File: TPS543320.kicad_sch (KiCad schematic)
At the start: 19 parts, among them U11 TPS543320RPYR

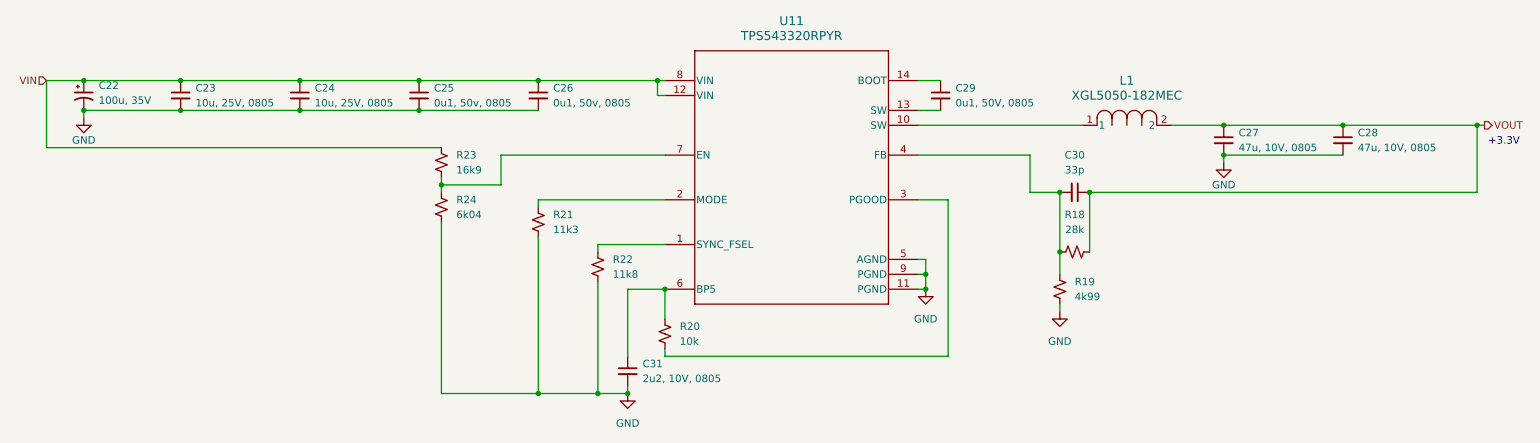
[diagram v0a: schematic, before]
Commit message: OBC: initial schematic entry complete
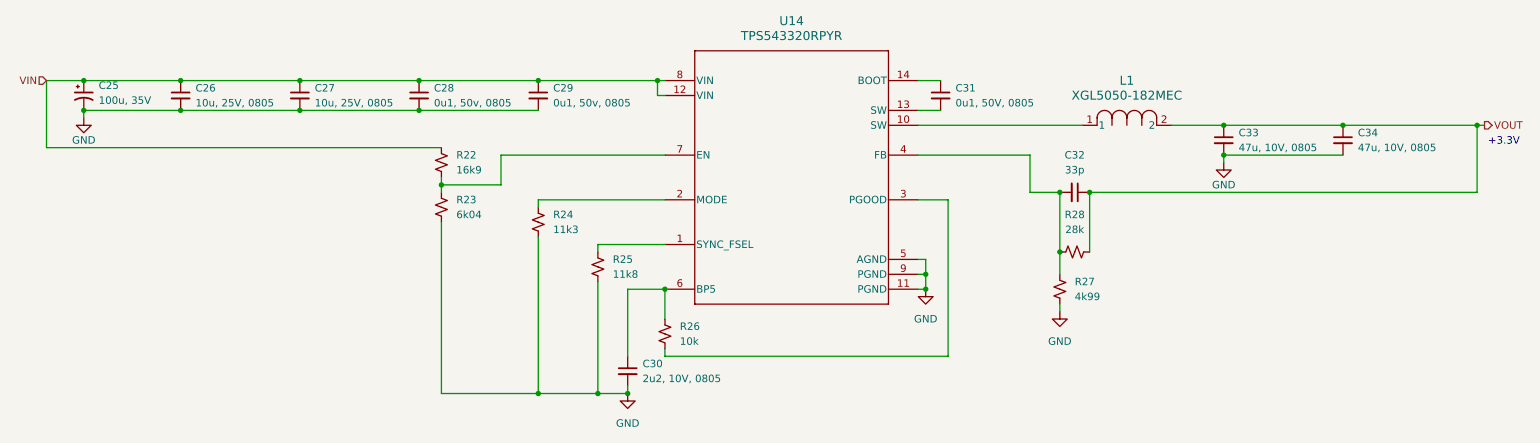
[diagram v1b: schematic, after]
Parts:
- C26: renamed from C23; footprint (none) -> Capacitor_SMD:C_0805_2012Metric
- C27: renamed from C24; footprint (none) -> Capacitor_SMD:C_0805_2012Metric
- C28: renamed from C25; footprint (none) -> Capacitor_SMD:C_0805_2012Metric
- C29: renamed from C26; footprint (none) -> Capacitor_SMD:C_0805_2012Metric
- C30: renamed from C31; footprint (none) -> Capacitor_SMD:C_0805_2012Metric
- C31: renamed from C29; footprint (none) -> Capacitor_SMD:C_0805_2012Metric
- C32: renamed from C30; footprint (none) -> Capacitor_SMD:C_0805_2012Metric
- C33: renamed from C27; footprint (none) -> Capacitor_SMD:C_0805_2012Metric
- C34: renamed from C28; footprint (none) -> Capacitor_SMD:C_0805_2012Metric
- R22: renamed from R23; footprint (none) -> Resistor_SMD:R_0805_2012Metric
- R23: renamed from R24; footprint (none) -> Resistor_SMD:R_0805_2012Metric
- R24: renamed from R21; footprint (none) -> Resistor_SMD:R_0805_2012Metric
- R25: renamed from R22; footprint (none) -> Resistor_SMD:R_0805_2012Metric
- R26: renamed from R20; footprint (none) -> Resistor_SMD:R_0805_2012Metric
- R27: renamed from R19; footprint (none) -> Resistor_SMD:R_0805_2012Metric
- R28: renamed from R18; footprint (none) -> Resistor_SMD:R_0805_2012Metric
- renumbered C22 to C25, U11 to U14

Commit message: OBC: preliminary layout
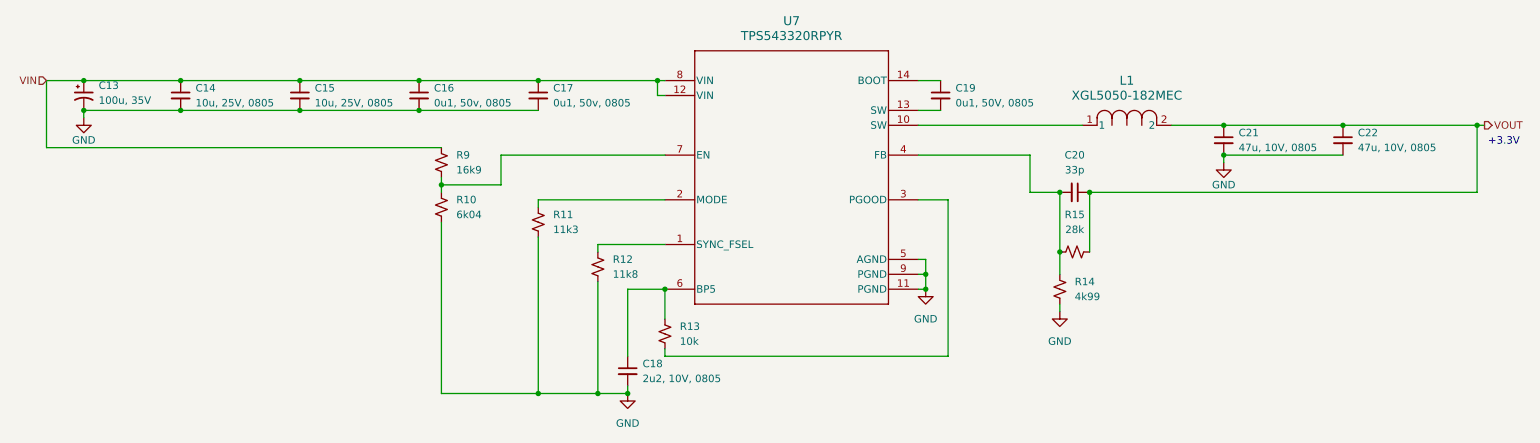
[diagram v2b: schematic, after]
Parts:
- C13: renamed from C25; footprint (none) -> Capacitor_SMD:C_0805_2012Metric
- L1: footprint IND_XGL5050_COC -> XGL5050-182MEC:IND_XGL5050_COC
- U7: renamed from U14; footprint RPY0014A-MFG -> TPS543320RPYR:RPY0014A-MFG
- renumbered C26 to C14, C27 to C15, C28 to C16, C29 to C17, C30 to C18, C31 to C19, C32 to C20, C33 to C21, C34 to C22, R23 to R10, R24 to R11, R25 to R12, R26 to R13, R27 to R14, R28 to R15, R22 to R9
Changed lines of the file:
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@@
 		(dnp no)
 		(fields_autoplaced yes)
-		(property "Reference" "C25"
+		(property "Reference" "C13"
 			(at 99.06 117.6781 0)
 			(effects
@@
 			)
 		)
-		(property "Footprint" ""
+		(property "Footprint" "Capacitor_SMD:C_0805_2012Metric"
 			(at 96.52 119.38 0)
 			(effects
@@
 			(project ""
 				(path "/ace5002f-3cbc-4a0a-869b-0e31ebd905b7/893aef5a-59ff-410b-9a71-9930aaf04e9f/e2cad078-3ca5-46c7-a65f-c1e6fb9d60cb"
-					(reference "C25")
+					(reference "C13")
 					(unit 1)
 				)
@@
 		(dnp no)
 		(fields_autoplaced yes)
-		(property "Reference" "R25"
+		(property "Reference" "R12"
 			(at 186.69 147.3199 0)
 			(effects
@@
 			(project ""
 				(path "/ace5002f-3cbc-4a0a-869b-0e31ebd905b7/893aef5a-59ff-410b-9a71-9930aaf04e9f/e2cad078-3ca5-46c7-a65f-c1e6fb9d60cb"
-					(reference "R25")
+					(reference "R12")
 					(unit 1)
 				)
@@
 		(dnp no)
 		(fields_autoplaced yes)
-		(property "Reference" "#PWR0102"
+		(property "Reference" "#PWR054"
 			(at 189.23 176.53 0)
 			(effects
@@
 			(project "Avionics"
 				(path "/ace5002f-3cbc-4a0a-869b-0e31ebd905b7/893aef5a-59ff-410b-9a71-9930aaf04e9f/e2cad078-3ca5-46c7-a65f-c1e6fb9d60cb"
-					(reference "#PWR0102")
+					(reference "#PWR054")
 					(unit 1)
 				)
@@
 		(dnp no)
 		(fields_autoplaced yes)
-		(property "Reference" "#PWR0104"
+		(property "Reference" "#PWR056"
 			(at 262.89 162.56 0)
 			(effects
@@
 			(project "Avionics"
 				(path "/ace5002f-3cbc-4a0a-869b-0e31ebd905b7/893aef5a-59ff-410b-9a71-9930aaf04e9f/e2cad078-3ca5-46c7-a65f-c1e6fb9d60cb"
-					(reference "#PWR0104")
+					(reference "#PWR056")
 					(unit 1)
 				)
@@
 		(dnp no)
 		(fields_autoplaced yes)
-		(property "Reference" "R23"
+		(property "Reference" "R10"
 			(at 160.02 137.1599 0)
 			(effects
@@
 			(project ""
 				(path "/ace5002f-3cbc-4a0a-869b-0e31ebd905b7/893aef5a-59ff-410b-9a71-9930aaf04e9f/e2cad078-3ca5-46c7-a65f-c1e6fb9d60cb"
-					(reference "R23")
+					(reference "R10")
 					(unit 1)
 				)
@@
 		(on_board yes)
 		(dnp no)
-		(property "Reference" "#PWR0101"
+		(property "Reference" "#PWR053"
 			(at 96.52 129.54 0)
 			(effects
@@
 			(project ""
 				(path "/ace5002f-3cbc-4a0a-869b-0e31ebd905b7/893aef5a-59ff-410b-9a71-9930aaf04e9f/e2cad078-3ca5-46c7-a65f-c1e6fb9d60cb"
-					(reference "#PWR0101")
+					(reference "#PWR053")
 					(unit 1)
 				)
@@
 		(dnp no)
 		(fields_autoplaced yes)
-		(property "Reference" "R24"
+		(property "Reference" "R11"
 			(at 176.53 139.6999 0)
 			(effects
@@
 			(project ""
 				(path "/ace5002f-3cbc-4a0a-869b-0e31ebd905b7/893aef5a-59ff-410b-9a71-9930aaf04e9f/e2cad078-3ca5-46c7-a65f-c1e6fb9d60cb"
-					(reference "R24")
+					(reference "R11")
 					(unit 1)
 				)
@@
 		(dnp no)
 		(fields_autoplaced yes)
-		(property "Reference" "C33"
+		(property "Reference" "C21"
 			(at 293.37 125.7362 0)
 			(effects
@@
 			(project ""
 				(path "/ace5002f-3cbc-4a0a-869b-0e31ebd905b7/893aef5a-59ff-410b-9a71-9930aaf04e9f/e2cad078-3ca5-46c7-a65f-c1e6fb9d60cb"
-					(reference "C33")
+					(reference "C21")
 					(unit 1)
 				)
@@
 		(dnp no)
 		(fields_autoplaced yes)
-		(property "Reference" "C31"
+		(property "Reference" "C19"
 			(at 245.11 118.1162 0)
 			(effects
@@
 			(project ""
 				(path "/ace5002f-3cbc-4a0a-869b-0e31ebd905b7/893aef5a-59ff-410b-9a71-9930aaf04e9f/e2cad078-3ca5-46c7-a65f-c1e6fb9d60cb"
-					(reference "C31")
+					(reference "C19")
 					(unit 1)
 				)
@@
 		(dnp no)
 		(fields_autoplaced yes)
-		(property "Reference" "R22"
+		(property "Reference" "R9"
 			(at 160.02 129.5399 0)
 			(effects
@@
 			(project ""
 				(path "/ace5002f-3cbc-4a0a-869b-0e31ebd905b7/893aef5a-59ff-410b-9a71-9930aaf04e9f/e2cad078-3ca5-46c7-a65f-c1e6fb9d60cb"
-					(reference "R22")
+					(reference "R9")
 					(unit 1)
 				)
@@
 		(dnp no)
 		(fields_autoplaced yes)
-		(property "Reference" "C30"
+		(property "Reference" "C18"
 			(at 191.77 165.1062 0)
 			(effects
@@
 			(project ""
 				(path "/ace5002f-3cbc-4a0a-869b-0e31ebd905b7/893aef5a-59ff-410b-9a71-9930aaf04e9f/e2cad078-3ca5-46c7-a65f-c1e6fb9d60cb"
-					(reference "C30")
+					(reference "C18")
 					(unit 1)
 				)
@@
 		(dnp no)
 		(fields_autoplaced yes)
-		(property "Reference" "C29"
+		(property "Reference" "C17"
 			(at 176.53 118.1162 0)
 			(effects
@@
 			(project ""
 				(path "/ace5002f-3cbc-4a0a-869b-0e31ebd905b7/893aef5a-59ff-410b-9a71-9930aaf04e9f/e2cad078-3ca5-46c7-a65f-c1e6fb9d60cb"
-					(reference "C29")
+					(reference "C17")
 					(unit 1)
 				)
@@
 		(dnp no)
 		(fields_autoplaced yes)
-		(property "Reference" "R28"
+		(property "Reference" "R15"
 			(at 265.43 139.7 90)
 			(effects
@@
 			(project ""
 				(path "/ace5002f-3cbc-4a0a-869b-0e31ebd905b7/893aef5a-59ff-410b-9a71-9930aaf04e9f/e2cad078-3ca5-46c7-a65f-c1e6fb9d60cb"
-					(reference "R28")
+					(reference "R15")
 					(unit 1)
 				)
@@
 		(dnp no)
 		(fields_autoplaced yes)
-		(property "Reference" "R27"
+		(property "Reference" "R14"
 			(at 265.43 151.1299 0)
 			(effects
@@
 			(project ""
 				(path "/ace5002f-3cbc-4a0a-869b-0e31ebd905b7/893aef5a-59ff-410b-9a71-9930aaf04e9f/e2cad078-3ca5-46c7-a65f-c1e6fb9d60cb"
-					(reference "R27")
+					(reference "R14")
 					(unit 1)
 				)
@@
 		(dnp no)
 		(fields_autoplaced yes)
-		(property "Reference" "U14"
+		(property "Reference" "U7"
 			(at 217.17 106.68 0)
 			(effects
@@
 			)
 		)
-		(property "Footprint" "RPY0014A-MFG"
+		(property "Footprint" "TPS543320RPYR:RPY0014A-MFG"
 			(at 195.58 116.84 0)
 			(effects
@@
 			(project "Avionics"
 				(path "/ace5002f-3cbc-4a0a-869b-0e31ebd905b7/893aef5a-59ff-410b-9a71-9930aaf04e9f/e2cad078-3ca5-46c7-a65f-c1e6fb9d60cb"
-					(reference "U14")
+					(reference "U7")
 					(unit 1)
 				)
@@
 		(on_board yes)
 		(dnp no)
-		(property "Reference" "#PWR0105"
+		(property "Reference" "#PWR057"
 			(at 290.83 137.16 0)
 			(effects
@@
 			(project ""
 				(path "/ace5002f-3cbc-4a0a-869b-0e31ebd905b7/893aef5a-59ff-410b-9a71-9930aaf04e9f/e2cad078-3ca5-46c7-a65f-c1e6fb9d60cb"
-					(reference "#PWR0105")
+					(reference "#PWR057")
 					(unit 1)
 				)
@@
 		(dnp no)
 		(fields_autoplaced yes)
-		(property "Reference" "C26"
+		(property "Reference" "C14"
 			(at 115.57 118.1162 0)
 			(effects
@@
 			(project ""
 				(path "/ace5002f-3cbc-4a0a-869b-0e31ebd905b7/893aef5a-59ff-410b-9a71-9930aaf04e9f/e2cad078-3ca5-46c7-a65f-c1e6fb9d60cb"
-					(reference "C26")
+					(reference "C14")
 					(unit 1)
 				)
@@
 		(dnp no)
 		(fields_autoplaced yes)
-		(property "Reference" "C32"
+		(property "Reference" "C20"
 			(at 265.4236 129.54 90)
 			(effects
@@
 			(project "Avionics"
 				(path "/ace5002f-3cbc-4a0a-869b-0e31ebd905b7/893aef5a-59ff-410b-9a71-9930aaf04e9f/e2cad078-3ca5-46c7-a65f-c1e6fb9d60cb"
-					(reference "C32")
+					(reference "C20")
 					(unit 1)
 				)
@@
 			)
 		)
-		(property "Footprint" "IND_XGL5050_COC"
+		(property "Footprint" "XGL5050-182MEC:IND_XGL5050_COC"
 			(at 281.94 124.46 0)
 			(effects
@@
 		(on_board yes)
 		(dnp no)
-		(property "Reference" "C28"
+		(property "Reference" "C16"
 			(at 156.21 118.1162 0)
 			(effects
@@
 			(project ""
 				(path "/ace5002f-3cbc-4a0a-869b-0e31ebd905b7/893aef5a-59ff-410b-9a71-9930aaf04e9f/e2cad078-3ca5-46c7-a65f-c1e6fb9d60cb"
-					(reference "C28")
+					(reference "C16")
 					(unit 1)
 				)
@@
 		(dnp no)
 		(fields_autoplaced yes)
-		(property "Reference" "C27"
+		(property "Reference" "C15"
 			(at 135.89 118.1162 0)
 			(effects
@@
 			(project ""
 				(path "/ace5002f-3cbc-4a0a-869b-0e31ebd905b7/893aef5a-59ff-410b-9a71-9930aaf04e9f/e2cad078-3ca5-46c7-a65f-c1e6fb9d60cb"
-					(reference "C27")
+					(reference "C15")
 					(unit 1)
 				)
@@
 		(dnp no)
 		(fields_autoplaced yes)
-		(property "Reference" "R26"
+		(property "Reference" "R13"
 			(at 198.12 158.7499 0)
 			(effects
@@
 			(project ""
 				(path "/ace5002f-3cbc-4a0a-869b-0e31ebd905b7/893aef5a-59ff-410b-9a71-9930aaf04e9f/e2cad078-3ca5-46c7-a65f-c1e6fb9d60cb"
-					(reference "R26")
+					(reference "R13")
 					(unit 1)
 				)
@@
 		(dnp no)
 		(fields_autoplaced yes)
-		(property "Reference" "C34"
+		(property "Reference" "C22"
 			(at 313.69 125.7362 0)
 			(effects
@@
 			(project ""
 				(path "/ace5002f-3cbc-4a0a-869b-0e31ebd905b7/893aef5a-59ff-410b-9a71-9930aaf04e9f/e2cad078-3ca5-46c7-a65f-c1e6fb9d60cb"
-					(reference "C34")
+					(reference "C22")
 					(unit 1)
 				)
@@
 		(dnp no)
 		(fields_autoplaced yes)
-		(property "Reference" "#PWR0103"
+		(property "Reference" "#PWR055"
 			(at 240.03 158.75 0)
 			(effects
@@
 			(project ""
 				(path "/ace5002f-3cbc-4a0a-869b-0e31ebd905b7/893aef5a-59ff-410b-9a71-9930aaf04e9f/e2cad078-3ca5-46c7-a65f-c1e6fb9d60cb"
-					(reference "#PWR0103")
-					(unit 1)
-				)
+					(reference "#PWR055")
+					(unit 1)
+				)

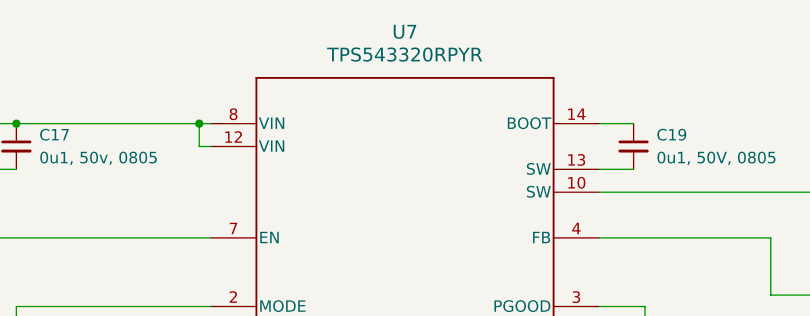
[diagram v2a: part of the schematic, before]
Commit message: OBC: start PCB layout
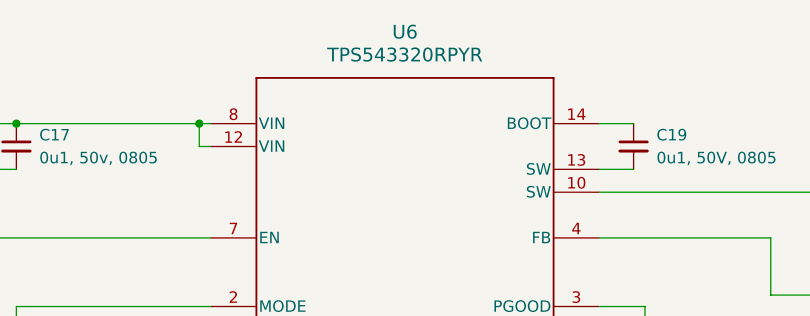
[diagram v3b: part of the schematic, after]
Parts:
- renumbered U7 to U6
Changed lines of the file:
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@@
 		(dnp no)
 		(fields_autoplaced yes)
-		(property "Reference" "#PWR054"
+		(property "Reference" "#PWR055"
 			(at 189.23 176.53 0)
 			(effects
@@
 			(project "Avionics"
 				(path "/ace5002f-3cbc-4a0a-869b-0e31ebd905b7/893aef5a-59ff-410b-9a71-9930aaf04e9f/e2cad078-3ca5-46c7-a65f-c1e6fb9d60cb"
-					(reference "#PWR054")
+					(reference "#PWR055")
 					(unit 1)
 				)
@@
 		(dnp no)
 		(fields_autoplaced yes)
-		(property "Reference" "#PWR056"
+		(property "Reference" "#PWR057"
 			(at 262.89 162.56 0)
 			(effects
@@
 			(project "Avionics"
 				(path "/ace5002f-3cbc-4a0a-869b-0e31ebd905b7/893aef5a-59ff-410b-9a71-9930aaf04e9f/e2cad078-3ca5-46c7-a65f-c1e6fb9d60cb"
-					(reference "#PWR056")
+					(reference "#PWR057")
 					(unit 1)
 				)
@@
 		(on_board yes)
 		(dnp no)
-		(property "Reference" "#PWR053"
+		(property "Reference" "#PWR054"
 			(at 96.52 129.54 0)
 			(effects
@@
 			(project ""
 				(path "/ace5002f-3cbc-4a0a-869b-0e31ebd905b7/893aef5a-59ff-410b-9a71-9930aaf04e9f/e2cad078-3ca5-46c7-a65f-c1e6fb9d60cb"
-					(reference "#PWR053")
+					(reference "#PWR054")
 					(unit 1)
 				)
@@
 		(dnp no)
 		(fields_autoplaced yes)
-		(property "Reference" "U7"
+		(property "Reference" "U6"
 			(at 217.17 106.68 0)
 			(effects
@@
 			(project "Avionics"
 				(path "/ace5002f-3cbc-4a0a-869b-0e31ebd905b7/893aef5a-59ff-410b-9a71-9930aaf04e9f/e2cad078-3ca5-46c7-a65f-c1e6fb9d60cb"
-					(reference "U7")
+					(reference "U6")
 					(unit 1)
 				)
@@
 		(on_board yes)
 		(dnp no)
-		(property "Reference" "#PWR057"
+		(property "Reference" "#PWR058"
 			(at 290.83 137.16 0)
 			(effects
@@
 			(project ""
 				(path "/ace5002f-3cbc-4a0a-869b-0e31ebd905b7/893aef5a-59ff-410b-9a71-9930aaf04e9f/e2cad078-3ca5-46c7-a65f-c1e6fb9d60cb"
-					(reference "#PWR057")
+					(reference "#PWR058")
 					(unit 1)
 				)
@@
 		(dnp no)
 		(fields_autoplaced yes)
-		(property "Reference" "#PWR055"
+		(property "Reference" "#PWR056"
 			(at 240.03 158.75 0)
 			(effects
@@
 			(project ""
 				(path "/ace5002f-3cbc-4a0a-869b-0e31ebd905b7/893aef5a-59ff-410b-9a71-9930aaf04e9f/e2cad078-3ca5-46c7-a65f-c1e6fb9d60cb"
-					(reference "#PWR055")
-					(unit 1)
-				)
+					(reference "#PWR056")
+					(unit 1)
+				)

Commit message: OBC: Continue PCB lauout
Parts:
- renumbered C14 to C10, C15 to C11, C16 to C12, C17 to C13, C18 to C14, C19 to C15, C20 to C16, C21 to C17, C22 to C18, C13 to C9, R9 to R11, R10 to R12, R11 to R13, R12 to R14, R13 to R15, R14 to R16, R15 to R17, U6 to U5

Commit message: Layout confirmed, PCBs ordered
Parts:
- C10, C11: DigiKey Part Number (none) -> 490-GRM21BZ71E106KE15KCT-ND
- C12, C13, C15: DigiKey Part Number (none) -> 399-C0805C104K5RACTUCT-ND
- C14: DigiKey Part Number (none) -> 1276-CL21B225KPFVPNECT-ND
- C16: DigiKey Part Number (none) -> 490-14776-1-ND
- C17, C18: DigiKey Part Number (none) -> 490-9961-1-ND
- C9: DigiKey Part Number (none) -> 399-C0805X104K5RAC7210CT-ND
- L1: DigiKey Part Number (none) -> 2457-XGL5050-182MEC-ND
- R11: DigiKey Part Number (none) -> 311-16.9KCRCT-ND
- R12: DigiKey Part Number (none) -> RMCF0805FT6K04CT-ND
- R13: DigiKey Part Number (none) -> 311-11.3KCRCT-ND
- R14: DigiKey Part Number (none) -> RMCF0805FT11K8CT-ND
- R15: DigiKey Part Number (none) -> 541-10.0KCCT-ND
- R16: DigiKey Part Number (none) -> TNP4.99KABCT-ND
- R17: DigiKey Part Number (none) -> 311-28.0KCRCT-ND
- U5: DigiKey Part Number (none) -> 296-TPS543320RPYRCT-ND
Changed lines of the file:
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@@
+			)
+		)
+		(property "DigiKey Part Number" "399-C0805X104K5RAC7210CT-ND"
+			(at 96.52 119.38 0)
+			(effects
+				(font
+					(size 1.27 1.27)
+				)
+				(hide yes)
 			)
 		)
@@
 			)
 		)
+		(property "DigiKey Part Number" "RMCF0805FT11K8CT-ND"
+			(at 184.15 148.59 0)
+			(effects
+				(font
+					(size 1.27 1.27)
+				)
+				(hide yes)
+			)
+		)
 		(pin "2"
 		)
@@
 			)
 		)
+		(property "DigiKey Part Number" "RMCF0805FT6K04CT-ND"
+			(at 157.48 138.43 0)
+			(effects
+				(font
+					(size 1.27 1.27)
+				)
+				(hide yes)
+			)
+		)
 		(pin "2"
 		)
@@
 			)
 		)
+		(property "DigiKey Part Number" "311-11.3KCRCT-ND"
+			(at 173.99 140.97 0)
+			(effects
+				(font
+					(size 1.27 1.27)
+				)
+				(hide yes)
+			)
+		)
 		(pin "2"
 		)
@@
 			)
 		)
+		(property "DigiKey Part Number" "490-9961-1-ND"
+			(at 290.83 127 0)
+			(effects
+				(font
+					(size 1.27 1.27)
+				)
+				(hide yes)
+			)
+		)
 		(pin "2"
 		)
@@
 			)
 		)
+		(property "DigiKey Part Number" "399-C0805C104K5RACTUCT-ND"
+			(at 242.57 119.38 0)
+			(effects
+				(font
+					(size 1.27 1.27)
+				)
+				(hide yes)
+			)
+		)
 		(pin "1"
 		)
@@
 			)
 		)
+		(property "DigiKey Part Number" "311-16.9KCRCT-ND"
+			(at 157.48 130.81 0)
+			(effects
+				(font
+					(size 1.27 1.27)
+				)
+				(hide yes)
+			)
+		)
 		(pin "2"
 		)
@@
 			)
 		)
+		(property "DigiKey Part Number" "1276-CL21B225KPFVPNECT-ND"
+			(at 189.23 166.37 0)
+			(effects
+				(font
+					(size 1.27 1.27)
+				)
+				(hide yes)
+			)
+		)
 		(pin "1"
 		)
@@
 			)
 		)
+		(property "DigiKey Part Number" "399-C0805C104K5RACTUCT-ND"
+			(at 173.99 119.38 0)
+			(effects
+				(font
+					(size 1.27 1.27)
+				)
+				(hide yes)
+			)
+		)
 		(pin "1"
 		)
@@
 			)
 		)
+		(property "DigiKey Part Number" "311-28.0KCRCT-ND"
+			(at 265.43 146.05 90)
+			(effects
+				(font
+					(size 1.27 1.27)
+				)
+				(hide yes)
+			)
+		)
 		(pin "2"
 		)
@@
 			)
 		)
+		(property "DigiKey Part Number" "TNP4.99KABCT-ND"
+			(at 262.89 152.4 0)
+			(effects
+				(font
+					(size 1.27 1.27)
+				)
+				(hide yes)
+			)
+		)
 		(pin "2"
 		)
@@
 			)
 		)
-		(property "Datasheet" "TPS543320RPYR"
+		(property "Datasheet" ""
 			(at 195.58 116.84 0)
 			(effects
@@
 		)
 		(property "SNAPEDA_PN" ""
+			(at 195.58 116.84 0)
+			(effects
+				(font
+					(size 1.27 1.27)
+				)
+				(hide yes)
+			)
+		)
+		(property "DigiKey Part Number" "296-TPS543320RPYRCT-ND"
 			(at 195.58 116.84 0)
 			(effects
@@
 			)
 		)
+		(property "DigiKey Part Number" "490-GRM21BZ71E106KE15KCT-ND"
+			(at 113.03 119.38 0)
+			(effects
+				(font
+					(size 1.27 1.27)
+				)
+				(hide yes)
+			)
+		)
 		(pin "1"
 		)
@@
 			)
 		)
+		(property "DigiKey Part Number" "490-14776-1-ND"
+			(at 265.43 135.89 90)
+			(effects
+				(font
+					(size 1.27 1.27)
+				)
+				(hide yes)
+			)
+		)
 		(pin "1"
 		)
@@
 			)
 		)
-		(property "Datasheet" "XGL5050-182MEC"
+		(property "Datasheet" ""
 			(at 281.94 124.46 0)
 			(effects
@@
 			)
 		)
+		(property "DigiKey Part Number" "2457-XGL5050-182MEC-ND"
+			(at 281.94 124.46 0)
+			(effects
+				(font
+					(size 1.27 1.27)
+				)
+				(hide yes)
+			)
+		)
 		(pin "2"
 		)
@@
 		)
 		(property "SNAPEDA_PN" ""
+			(at 153.67 119.38 0)
+			(effects
+				(font
+					(size 1.27 1.27)
+				)
+				(hide yes)
+			)
+		)
+		(property "DigiKey Part Number" "399-C0805C104K5RACTUCT-ND"
 			(at 153.67 119.38 0)
 			(effects
@@
 			)
 		)
+		(property "DigiKey Part Number" "490-GRM21BZ71E106KE15KCT-ND"
+			(at 133.35 119.38 0)
+			(effects
+				(font
+					(size 1.27 1.27)
+				)
+				(hide yes)
+			)
+		)
 		(pin "1"
 		)
@@
 			)
 		)
+		(property "DigiKey Part Number" "541-10.0KCCT-ND"
+			(at 195.58 160.02 0)
+			(effects
+				(font
+					(size 1.27 1.27)
+				)
+				(hide yes)
+			)
+		)
 		(pin "2"
 		)
@@
 			(at 311.15 127 0)
 			(effects
+				(font
+					(size 1.27 1.27)
+				)
+				(hide yes)
+			)
+		)
+		(property "DigiKey Part Number" "490-9961-1-ND"
+			(at 311.15 127 0)
+			(effects
